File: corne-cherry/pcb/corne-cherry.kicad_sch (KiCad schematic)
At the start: 146 parts, among them J1 MJ-4PP-9, J2 OLED, J3 MJ-4PP-9, J4 OLED, SW1 SW_PUSH, SW10 SW_PUSH, SW11 SW_PUSH, SW12 SW_PUSH, SW13 SW_PUSH, SW14 SW_PUSH, SW15 SW_PUSH, SW16 SW_PUSH, SW17 SW_PUSH, SW18 SW_PUSH, SW19 SW_PUSH, SW2 SW_PUSH, SW20 SW_PUSH, SW21 SW_PUSH, SW22 SW_PUSH, SW23 SW_PUSH, SW24 SW_PUSH, SW25 SW_PUSH, SW26 SW_PUSH, SW27 SW_PUSH, SW28 SW_PUSH, SW29 SW_PUSH, SW3 SW_PUSH, SW30 SW_PUSH, SW31 SW_PUSH, SW32 SW_PUSH, SW33 SW_PUSH, SW34 SW_PUSH, SW35 SW_PUSH, SW36 SW_PUSH, SW37 SW_PUSH, SW38 SW_PUSH, SW39 SW_PUSH, SW4 SW_PUSH, SW40 SW_PUSH, SW41 SW_PUSH, SW42 SW_PUSH, SW5 SW_PUSH, SW6 SW_PUSH, SW7 SW_PUSH, SW8 SW_PUSH, SW9 SW_PUSH, U1 ProMicro, U2 ProMicro

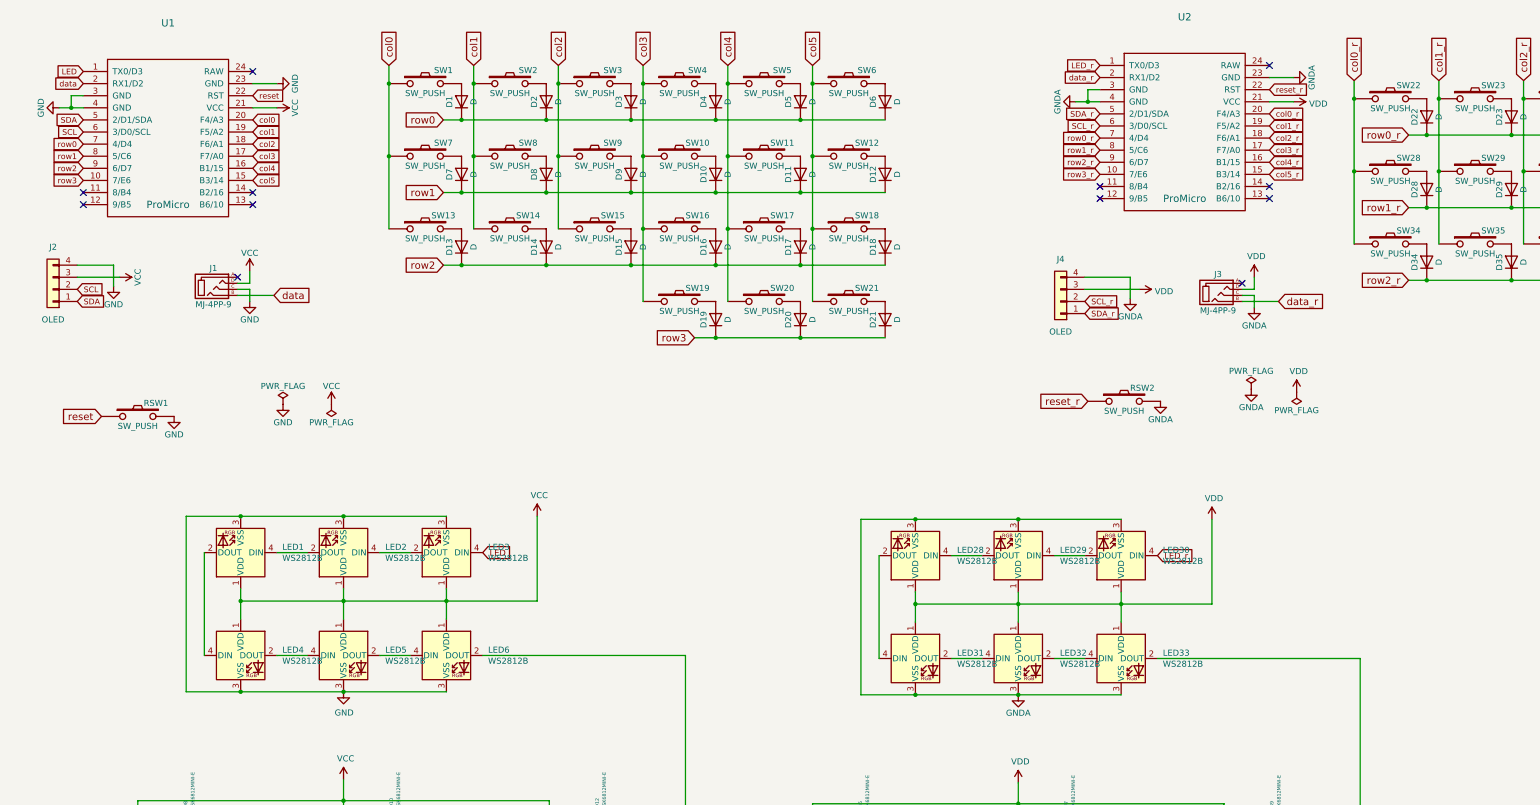
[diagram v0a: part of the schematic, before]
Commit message: Add wireless powers and switches and remove underlights
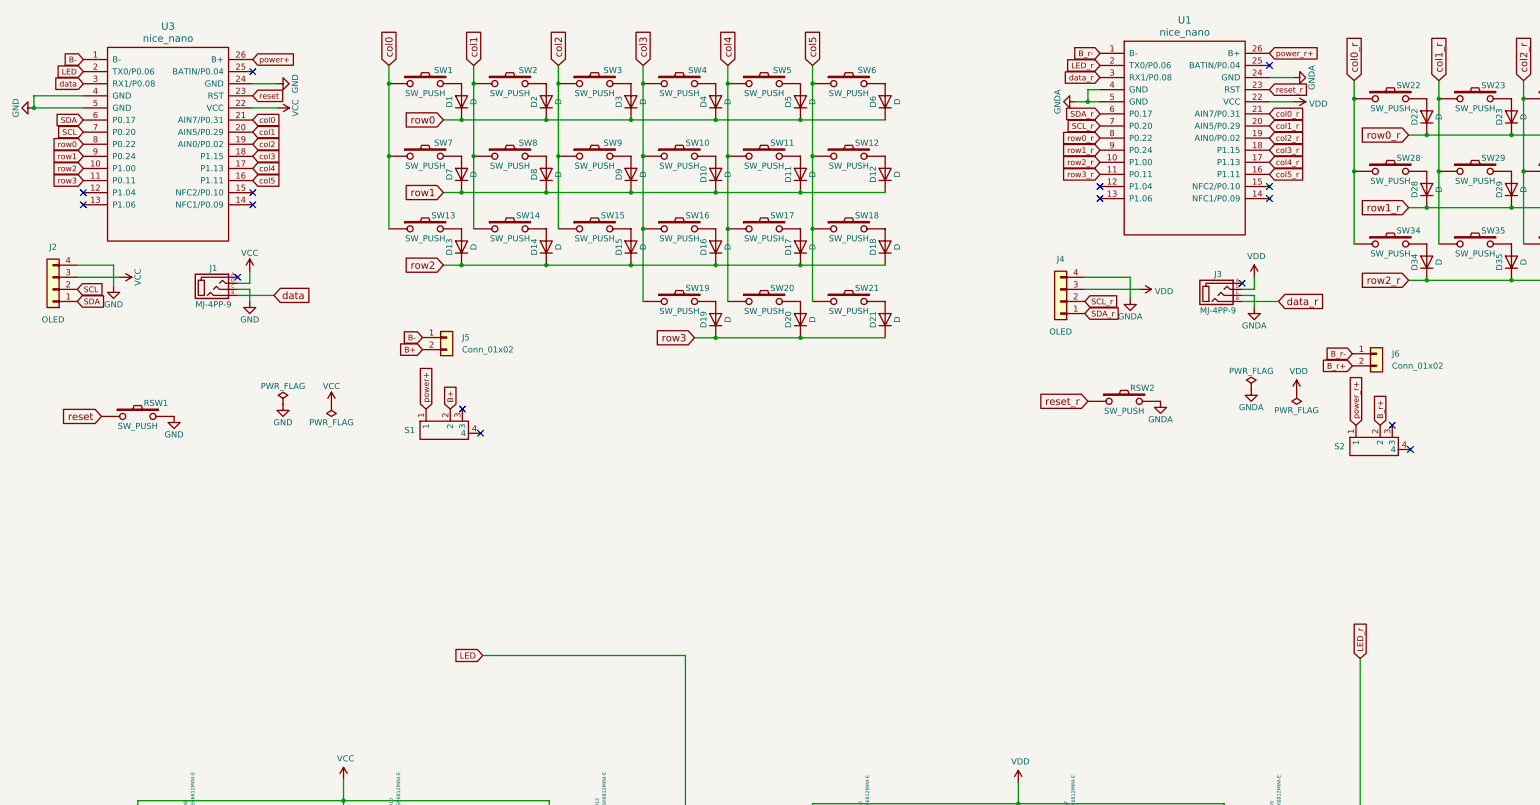
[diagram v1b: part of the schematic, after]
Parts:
- removed LED1, LED2, LED28, LED29, LED3, LED30, LED31, LED32, LED33, LED4, LED5, LED6: WS2812B, LED_SMD:LED_WS2812B_PLCC4_5.0x5.0mm_P3.2mm, symbol LED:WS2812B
- removed U1, U2: ProMicro, kbd:ProMicro_v3, symbol kbd:ProMicro
- added J5, J6: Conn_01x02, Connector_PinSocket_2.54mm:PinSocket_1x02_P2.54mm_Vertical, symbol Connector_Generic:Conn_01x02
- added S1, S2: ~, switch:SW-SMD_MSK12C02-HB, symbol Switch:HX_MSK12C02-HB
- added U1, U3: nice_nano, nice-nano-kicad:nice_nano, symbol nice_nano:nice_nano
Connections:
- net GND: now also U3.24 (GND), U3.4 (GND), U3.5 (GND)
- net GNDA: now also U1.24 (GND), U1.4 (GND), U1.5 (GND)
- net LED: now also LED27.4 (DIN), U3.2 (TX0/P0.06)
- net LED_r: now also LED54.4 (DIN), U1.2 (TX0/P0.06)
- net SCL: now also U3.7 (P0.20)
- net SCL_r: now also U1.7 (P0.20)
- net SDA: now also U3.6 (P0.17)
- net SDA_r: now also U1.6 (P0.17)
- net VCC: now also U3.22 (VCC)
- net VDD: now also U1.22 (VCC)
- net col0: now also U3.21 (AIN7/P0.31)
- net col0_r: now also U1.21 (AIN7/P0.31)
- net col1: now also U3.20 (AIN5/P0.29)
- net col1_r: now also U1.20 (AIN5/P0.29)
- net col2: now also U3.19 (AIN0/P0.02)
- net col2_r: now also U1.19 (AIN0/P0.02)
- net col3: now also U3.18 (P1.15)
- net col3_r: now also U1.18 (P1.15)
- net col4: now also U3.17 (P1.13)
- net col4_r: now also U1.17 (P1.13)
- net col5: now also U3.16 (P1.11)
- net col5_r: now also U1.16 (P1.11)
- net data: now also U3.3 (RX1/P0.08)
- net data_r: now also U1.3 (RX1/P0.08)
- net reset: now also U3.23 (RST)
- net reset_r: now also U1.23 (RST)
- net row0: now also U3.8 (P0.22)
- net row0_r: now also U1.8 (P0.22)
- net row1: now also U3.9 (P0.24)
- net row1_r: now also U1.9 (P0.24)
- net row2: now also U3.10 (P1.00)
- net row2_r: now also U1.10 (P1.00)
- net row3: now also U3.11 (P0.11)
- net row3_r: now also U1.11 (P0.11)
- new net B+: J5.2 (Pin_2), S1.2
- new net B-: J5.1 (Pin_1), U3.1 (B-)
- new net B_r+: J6.2 (Pin_2), S2.2
- new net B_r-: J6.1 (Pin_1), U1.1 (B-)
- new net power+: S1.1, U3.26 (B+)
- new net power_r+: S2.1, U1.26 (B+)
- no-connect marks 14 -> 18
